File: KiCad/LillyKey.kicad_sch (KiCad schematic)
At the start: 62 parts, among them J1 Conn_01x02_Socket, SW1 SW_Push, SW10 SW_Push, SW11 SW_Push, SW12 SW_Push, SW13 SW_Push, SW14 SW_Push, SW15 SW_Push, SW16 SW_Push, SW17 SW_Push, SW18 SW_Push, SW19 SW_Push, SW2 SW_Push, SW20 SW_Push, SW21 SW_Push, SW22 SW_Push, SW23 SW_Push, SW24 SW_Push, SW25 SW_Push, SW26 SW_Push, SW27 SW_Push, SW28 SW_Push, SW29 SW_Push, SW3 SW_Push, SW30 SW_Push, SW4 SW_Push, SW5 SW_Push, SW6 SW_Push, SW7 SW_Push, SW8 SW_Push, SW9 SW_Push, U2 XIAO-nRF52840-SMD

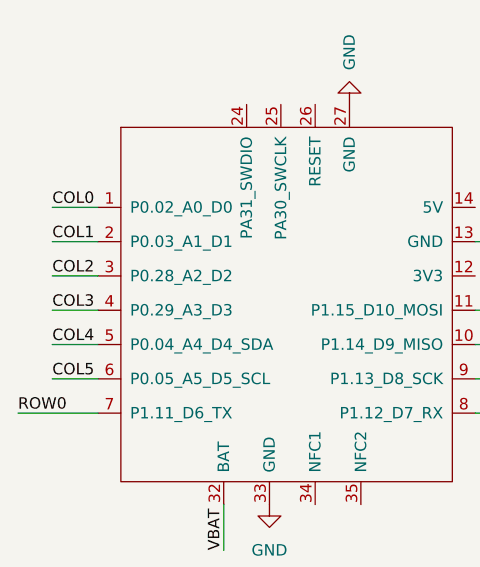
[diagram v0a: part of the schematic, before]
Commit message: Fliped around keys, cleanup
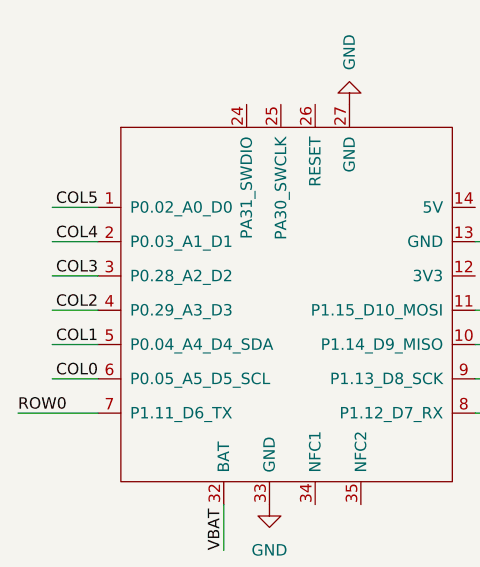
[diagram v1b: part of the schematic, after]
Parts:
- D1, D10, D11, D12, D13, D14, D15, D16, D17, D18, D19, D2, D20, D21, D22, D23, D24, D25, D26, D27, D28, D29, D3, D30, D4, D5, D6, D7, D8, D9: footprint ExtraFootprints:RevDiode -> Footprints:RevDiode
- J1: footprint ExtraFootprints:JSTPH -> Footprints:JSTPH
- SW1, SW10, SW11, SW12, SW13, SW14, SW15, SW16, SW17, SW18, SW19, SW2, SW20, SW21, SW22, SW23, SW24, SW25, SW26, SW27, SW28, SW29, SW3, SW30, SW4, SW5, SW6, SW7, SW8, SW9: footprint ExtraFootprints:SW_Hotswap_Kailh_Choc_V1V2 -> Footprints:SW_Hotswap_Kailh_Choc_V1V2
- U2: footprint ExtraFootprints:XIAO_nRF52840_DUAL -> Footprints:XIAO_nRF52840_DUAL
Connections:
- net COL0: now also U2.6 (P0.05_A5_D5_SCL); no longer U2.1 (P0.02_A0_D0)
- net COL1: now also U2.5 (P0.04_A4_D4_SDA); no longer U2.2 (P0.03_A1_D1)
- net COL2: now also U2.4 (P0.29_A3_D3); no longer U2.3 (P0.28_A2_D2)
- net COL3: now also U2.3 (P0.28_A2_D2); no longer U2.4 (P0.29_A3_D3)
- net COL4: now also U2.2 (P0.03_A1_D1); no longer U2.5 (P0.04_A4_D4_SDA)
- net COL5: now also U2.1 (P0.02_A0_D0); no longer U2.6 (P0.05_A5_D5_SCL)
